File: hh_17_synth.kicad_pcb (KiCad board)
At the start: 2 copper layers, 90 x 40 mm, 0 parts

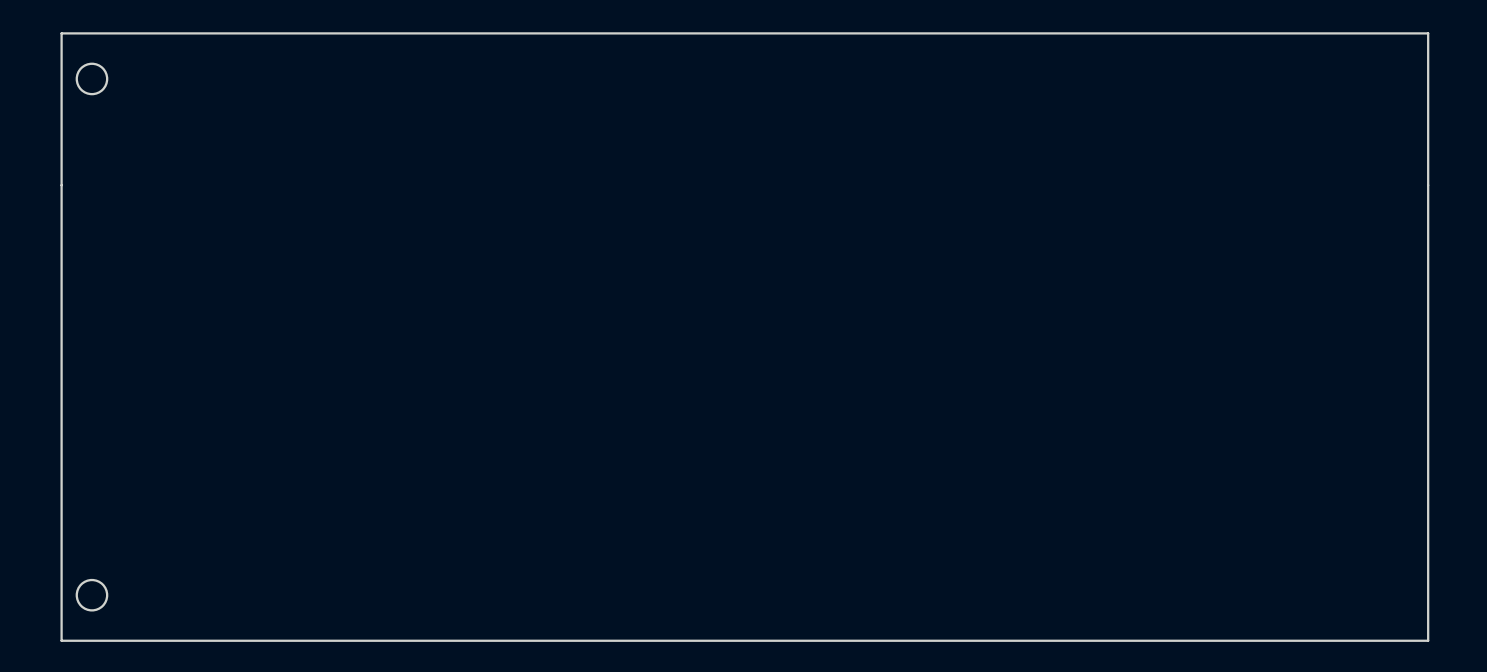
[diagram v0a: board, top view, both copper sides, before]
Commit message: Imported Mitch's touchpad and keyboard lib/mod
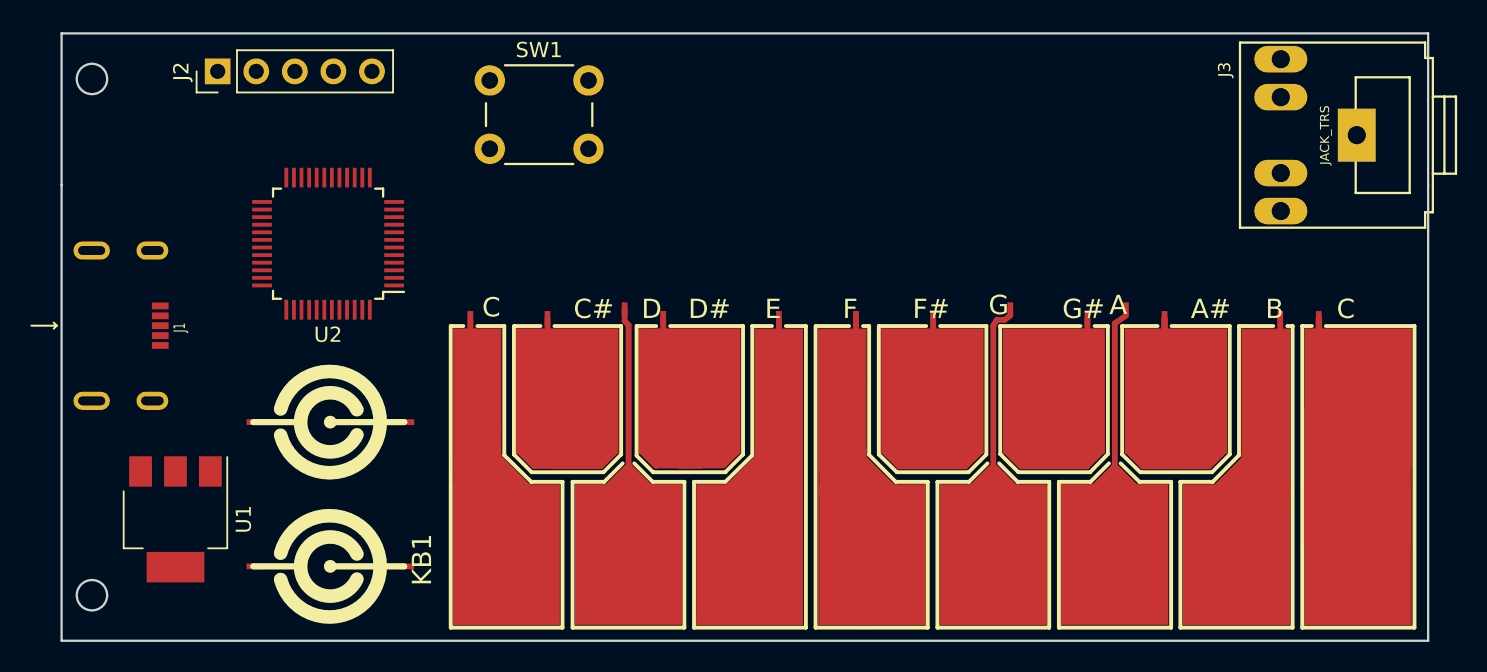
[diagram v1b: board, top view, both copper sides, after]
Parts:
- added J1: USB_OTG, custom:HDMI_476420001_CONN, F.Cu at (71.5, 69.2)
- added J2: debug, Pin_Headers:Pin_Header_Straight_1x05_Pitch2.54mm, F.Cu at (75.3, 52.5)
- added J3: JACK_TRS, custom:Tayda_3.5mm_stereo_TRS_jack_A-853, F.Cu at (148.7, 56.7)
- added KB1: MITCH-PARTS_PCB-KEYBOARD2, custom:MITCH-PARTS_PCB-KEYBOARD2_kicad_fix, F.Cu at (122.4, 79.0)
- added SW1: SW_Push, Buttons_Switches_ThroughHole:SW_PUSH_6mm, F.Cu at (93.2, 53.1)
- added TOUCH1: MITCH-PARTS_PCB-TOUCHPAD2, MITCH-PARTS_PCB-TOUCHPAD2, F.Cu at (82.7, 75.6)
- added TOUCH2: MITCH-PARTS_PCB-TOUCHPAD2, MITCH-PARTS_PCB-TOUCHPAD2, F.Cu at (82.7, 85.1)
- added U1: LM1117-3.3, TO_SOT_Packages_SMD:SOT-223, F.Cu at (72.5, 82.0)
- added U2: STM32F072CBTx, Housings_QFP:LQFP-48_7x7mm_Pitch0.5mm, F.Cu at (82.5, 63.9)
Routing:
- net /D#: track 0.00 -> 20.6 mm
- net /C: track 0.00 -> 20.0 mm
- net /E: track 0.00 -> 17.3 mm
- net /F: track 0.00 -> 17.1 mm
- net /C#: track 0.00 -> 16.6 mm
- net /D: track 0.00 -> 16.3 mm

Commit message: placed parts, changed some footprints.
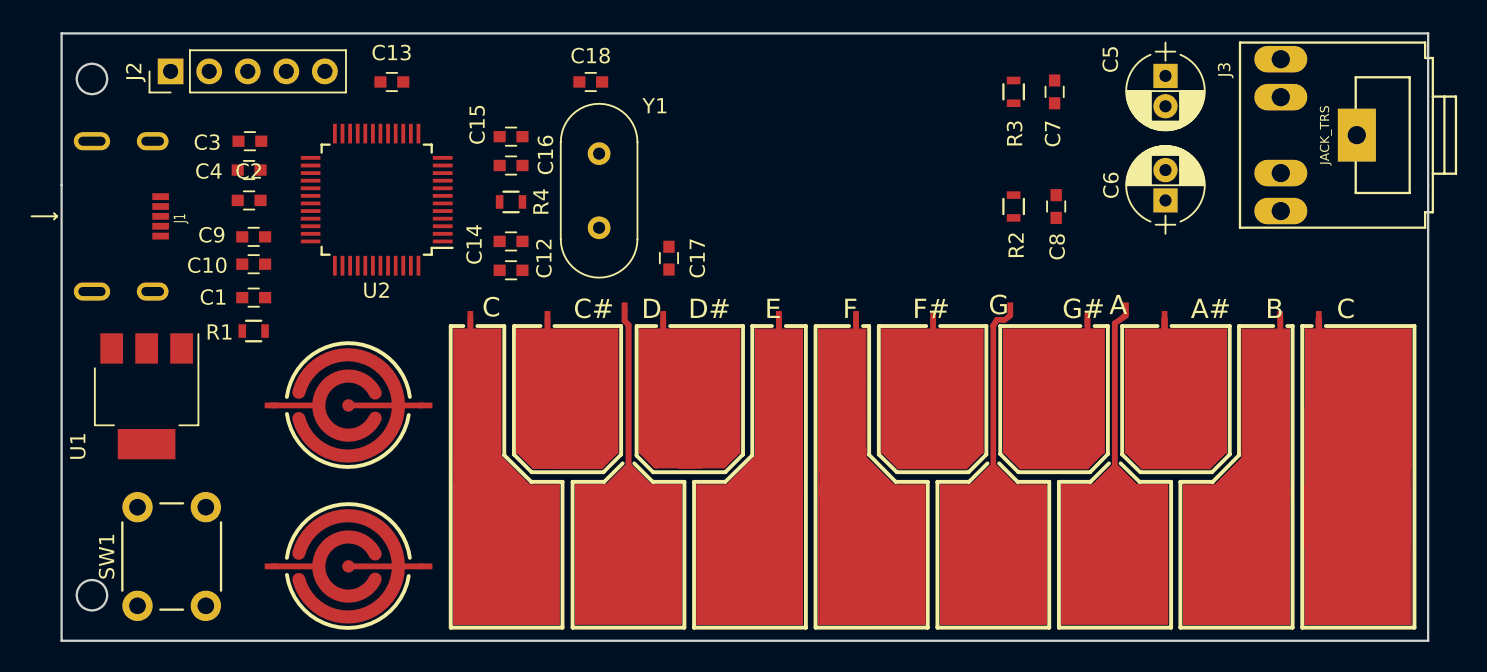
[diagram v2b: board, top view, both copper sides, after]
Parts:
- added C1: 1uF, Capacitors_SMD:C_0603, F.Cu at (77.7, 67.4)
- added C10: 4.7uF, Capacitors_SMD:C_0603, F.Cu at (77.7, 65.2)
- added C12: 100nF, Capacitors_SMD:C_0603, F.Cu at (94.6, 65.6)
- added C13: 100nF, Capacitors_SMD:C_0603, F.Cu at (86.8, 53.2)
- added C14: 4.7uF, Capacitors_SMD:C_0603, F.Cu at (94.6, 63.7)
- added C15: 1uF, Capacitors_SMD:C_0603, F.Cu at (94.6, 56.8)
- added C16: 10nF, Capacitors_SMD:C_0603, F.Cu at (94.6, 58.7)
- added C17: 27pF, Capacitors_SMD:C_0603, F.Cu at (105.0, 64.8)
- added C18: 27pF, Capacitors_SMD:C_0603, F.Cu at (99.8, 53.2)
- added C2: 1uF, Capacitors_SMD:C_0603, F.Cu at (77.3, 61.0)
- added C3: 100nF, Capacitors_SMD:C_0603, F.Cu at (77.4, 57.1)
- added C4: 10nF, Capacitors_SMD:C_0603, F.Cu at (77.3, 59.0)
- added C5: 1uF, Capacitors_ThroughHole:CP_Radial_D5.0mm_P2.00mm, F.Cu at (137.7, 52.8)
- added C6: 1uF, Capacitors_ThroughHole:CP_Radial_D5.0mm_P2.00mm, F.Cu at (137.7, 61.0)
- added C7: 0.1uF, Capacitors_SMD:C_0603, F.Cu at (130.4, 53.9)
- added C8: 0.1uF, Capacitors_SMD:C_0603, F.Cu at (130.5, 61.4)
- added C9: 100nF, Capacitors_SMD:C_0603, F.Cu at (77.7, 63.4)
- added R1: 10k, Resistors_SMD:R_0603, F.Cu at (77.7, 69.6)
- added R2: 8, Resistors_SMD:R_0603, F.Cu at (127.7, 61.4)
- added R3: 8, Resistors_SMD:R_0603, F.Cu at (127.7, 53.9)
- added R4: 220E, Resistors_SMD:R_0603, F.Cu at (94.6, 61.1)
- added Y1: 16MHz, Crystals:Crystal_HC49-4H_Vertical, F.Cu at (100.4, 62.8)
- TOUCH1, TOUCH2: footprint MITCH-PARTS_PCB-TOUCHPAD2 -> custom:MITCH-PARTS_PCB-TOUCHPAD2_kicad_fix
- moved SW1 41.7 mm to (70.0, 87.7), turned to 90 degrees
- moved U1 8.32 mm to (70.6, 73.9)
- moved J1 7.20 mm to (71.5, 62.0)
- moved U2 4.32 mm to (85.8, 61.0)
- moved J2 3.10 mm to (72.2, 52.5)
- moved TOUCH1 1.63 mm to (83.9, 74.5)
- moved TOUCH2 1.20 mm to (83.9, 85.1)
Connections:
- J3 pad 2: (no net) -> Net-(C8-Pad1)
- J3 pad 3: (no net) -> Net-(C7-Pad1)
- U2 pad 14: (no net) -> /DAC_C1
- U2 pad 15: (no net) -> /DAC_C2
- U2 pad 5: (no net) -> /OSC_IN
- U2 pad 6: (no net) -> /OSC_OUT
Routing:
- net /G: track 0.00 -> 16.9 mm
- net /B: track 0.00 -> 16.7 mm
- net /C+: track 0.00 -> 16.7 mm
- net /A: track 0.00 -> 16.5 mm
- net /F#: track 0.00 -> 14.4 mm
- net /A#: track 0.00 -> 13.3 mm
- net /G#: track 0.00 -> 9.46 mm

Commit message: finished layout etc.
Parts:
- moved SW1 15.0 mm to (68.2, 72.8), turned to 0 degrees
- moved U1 11.7 mm to (74.2, 85.0)
- moved C18 6.82 mm to (104.8, 58.0), turned to 90 degrees
- moved R1 5.34 mm to (82.8, 68.2)
- moved C8 3.24 mm to (133.4, 60.0)
- moved R2 3.20 mm to (130.6, 60.0)
- moved C7 2.90 mm to (133.3, 53.9)
- moved R3 2.90 mm to (130.6, 53.9)
- moved C17 1.27 mm to (104.8, 63.5)
- moved C13 1.17 mm to (86.0, 52.4)
- moved C5 0.57 mm to (138.1, 52.4)
- moved C6 0.36 mm to (138.1, 60.9)
- moved J3 0.34 mm to (148.4, 56.5)
- moved C2 0.25 mm to (77.6, 61.0), turned to 180 degrees
- moved C3 0.25 mm to (77.7, 57.1), turned to 180 degrees
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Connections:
- net /USB_DM renamed /USB_D_N
- net /USB_DP renamed /USB_D_P
- R2 pad 2: /DAC_C2 -> /DAC_C1
- R3 pad 2: /DAC_C1 -> /DAC_C2
- SW1 pad 2: Net-(SW1-Pad2) -> /VDD
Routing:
- net /VDD: track 0.00 -> 114.1 mm, vias 0 -> 5
- net /C+: track 16.7 -> 98.4 mm, vias 0 -> 2
- net /B: track 16.7 -> 96.0 mm, vias 0 -> 2
- net /A#: track 13.3 -> 83.4 mm, vias 0 -> 2
- net GND: track 0.00 -> 62.9 mm, vias 0 -> 28
- net /A: track 16.5 -> 79.0 mm, vias 0 -> 2
- net /E: track 17.3 -> 78.7 mm, vias 0 -> 2
- net /G#: track 9.46 -> 69.1 mm, vias 0 -> 2
- net /F: track 17.1 -> 76.2 mm, vias 0 -> 2
- net /G: track 16.9 -> 74.4 mm, vias 0 -> 2
- net /C: track 20.0 -> 77.0 mm, vias 0 -> 2
- net /F#: track 14.4 -> 70.8 mm, vias 0 -> 2
- net /C#: track 16.6 -> 68.3 mm, vias 0 -> 2
- net /D#: track 20.6 -> 72.2 mm, vias 0 -> 2
- net /DAC_C1: track 0.00 -> 46.2 mm
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- added copper zone on B.Cu, net /VBUS
- added copper zone on F.Cu, net /VBUS
- added copper zone on F.Cu, net /VDD
- added copper zone on B.Cu, net GND
- added copper zone on F.Cu, net GND
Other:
- outline, holes or cut-outs redrawn
- net class Default: clearance 0.2 -> 0.15
- rule trace_clearance: 0.2 -> 0.15

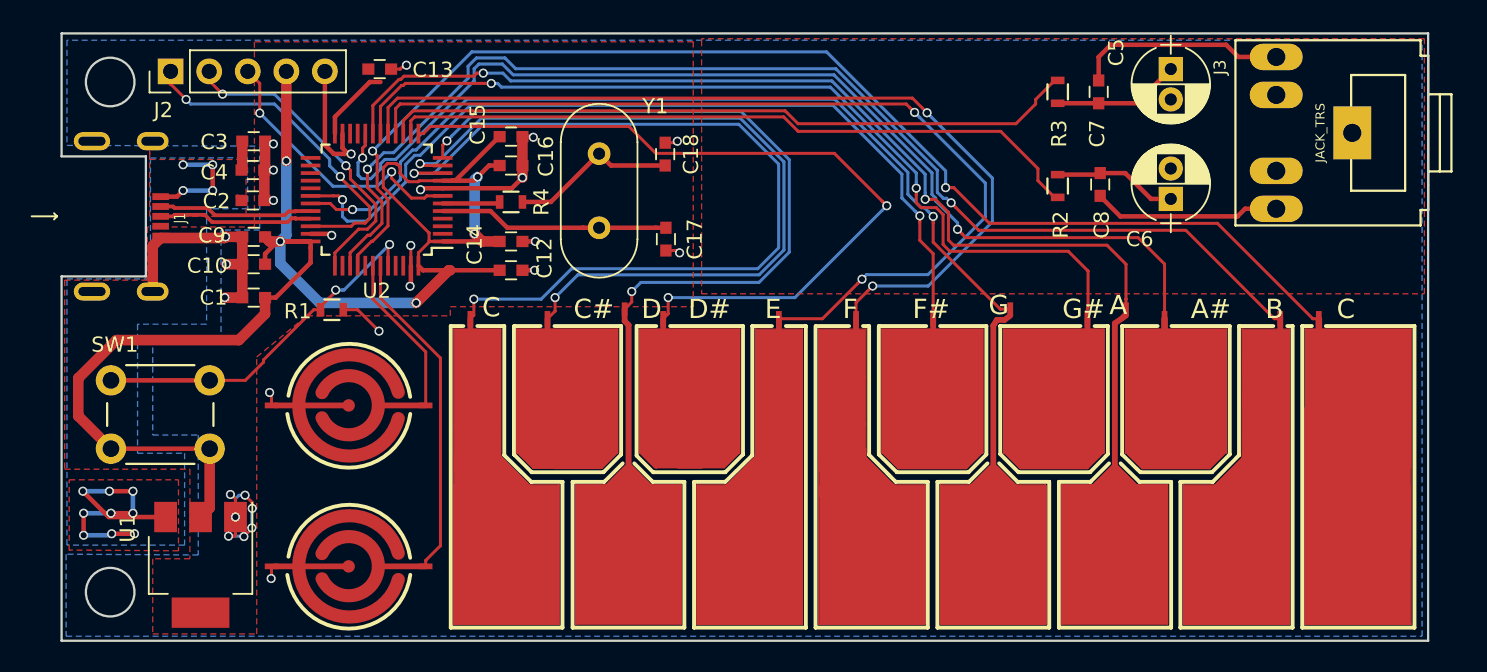
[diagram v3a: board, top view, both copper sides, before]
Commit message: updated layout with buttons/pots
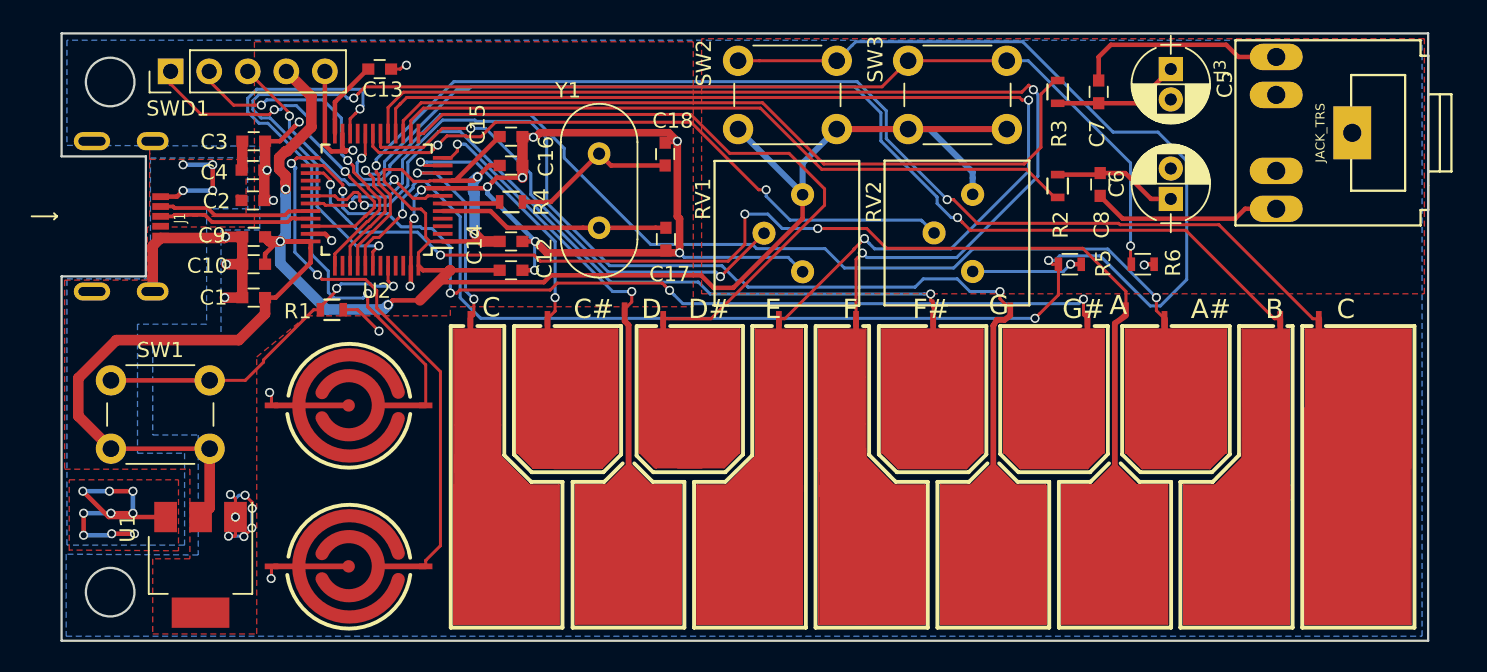
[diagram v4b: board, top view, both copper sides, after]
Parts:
- removed J2: debug, Pin_Headers:Pin_Header_Straight_1x05_Pitch2.54mm
- added R5: 10k, Resistors_SMD:R_0603, F.Cu at (131.4, 65.2)
- added R6: 10k, Resistors_SMD:R_0603, F.Cu at (136.2, 65.2)
- added RV1: POT, custom:3386P-1-T, F.Cu at (112.8, 63.2)
- added RV2: POT, custom:3386P-1-T, F.Cu at (124.0, 63.1)
- added SW2: SW_Push, Buttons_Switches_THT:SW_PUSH_6mm, F.Cu at (109.5, 51.8)
- added SW3: SW_Push, Buttons_Switches_THT:SW_PUSH_6mm, F.Cu at (120.8, 51.8)
- added SWD1: debug, Pin_Headers:Pin_Header_Straight_1x05_Pitch2.54mm, F.Cu at (72.2, 52.5)
- C5, C6: footprint Capacitors_ThroughHole:CP_Radial_D5.0mm_P2.00mm -> Capacitors_THT:CP_Radial_D5.0mm_P2.00mm
- SW1: footprint Buttons_Switches_ThroughHole:SW_PUSH_6mm -> Buttons_Switches_THT:SW_PUSH_6mm
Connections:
- net /VDD renamed VDD
- U2 pad 18: /G# -> /PT1
- U2 pad 19: /A -> /PT2
- U2 pad 22: (no net) -> /TB1
- U2 pad 25: (no net) -> /TB2
- U2 pad 26: (no net) -> /G#
- U2 pad 27: (no net) -> /A
- U2 pad 41: (no net) -> /PB1
- U2 pad 42: /TB1 -> /PB2
- U2 pad 43: /TB2 -> (no net)
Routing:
- net /PB1: track 0.00 -> 112.1 mm, vias 0 -> 3
- net /PB2: track 0.00 -> 84.2 mm, vias 0 -> 3
- net VDD: track 114.1 -> 175.2 mm
- net GND: track 62.9 -> 119.5 mm, vias 28 -> 31
- net /C: track 77.0 -> 34.0 mm
- net /PT2: track 0.00 -> 42.1 mm, vias 0 -> 2
- net /C#: track 68.3 -> 34.4 mm
- net /PT1: track 0.00 -> 32.7 mm, vias 0 -> 2
- net /TB1: track 10.6 -> 38.3 mm, vias 0 -> 2
- net /D: track 61.1 -> 34.8 mm
- net /TB2: track 21.8 -> 34.2 mm, vias 0 -> 2
- net /F: track 76.2 -> 86.3 mm
- net /E: track 78.7 -> 86.7 mm
- net /D#: track 72.2 -> 64.7 mm, vias 2 -> 0
- net /F#: track 70.8 -> 65.6 mm
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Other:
- board text added: "HILLHACKS '17"

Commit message: added audio amp, uart port, leds
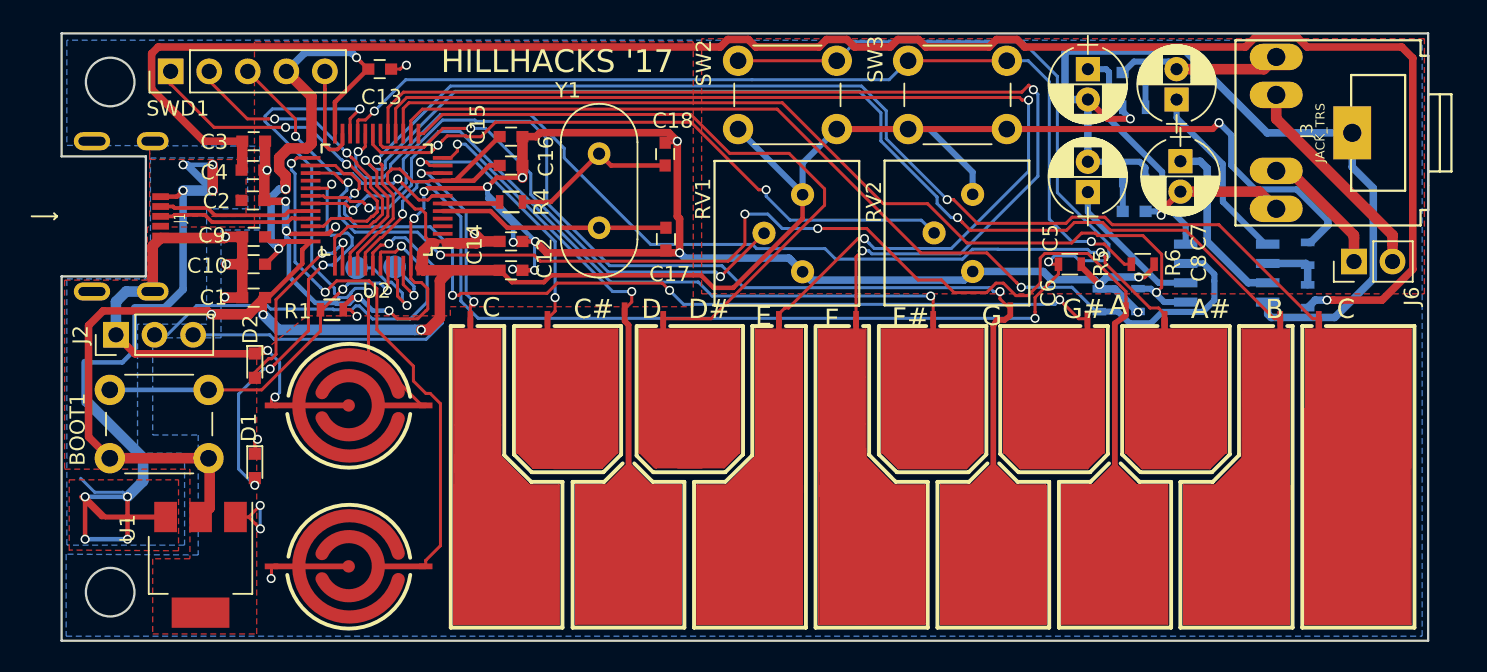
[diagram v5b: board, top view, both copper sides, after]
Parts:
- removed SW1: SW_Push, Buttons_Switches_THT:SW_PUSH_6mm
- added BOOT1: SW_Push, Buttons_Switches_THT:SW_PUSH_6mm, F.Cu at (68.2, 73.5)
- added C11: 0.1uF, Capacitors_SMD:C_0603, B.Cu at (135.6, 52.6)
- added C19: 0.1uF, Capacitors_SMD:C_0603, B.Cu at (135.6, 61.7)
- added D1: LED, LEDs:LED_0603, F.Cu at (77.7, 78.5)
- added D2: LED, LEDs:LED_0603, F.Cu at (77.7, 71.9)
- added J2: serial, Pin_Headers:Pin_Header_Straight_1x03_Pitch2.54mm, F.Cu at (68.6, 69.8)
- added J4: SCL, Measurement_Points:Measurement_Point_Round-SMD-Pad_Small, B.Cu at (84.4, 65.4)
- added J5: SDA, Measurement_Points:Measurement_Point_Round-SMD-Pad_Small, B.Cu at (86.9, 65.4)
- added J6: out, Pin_Headers:Pin_Header_Straight_1x02_Pitch2.54mm, F.Cu at (150.1, 65.0)
- added R10: 4.7, Resistors_SMD:R_0603, B.Cu at (135.6, 59.7)
- added R7: 0E, Resistors_SMD:R_0603, B.Cu at (147.1, 64.5)
- added R8: NC, Resistors_SMD:R_0603, B.Cu at (147.1, 67.3)
- added R9: 4.7, Resistors_SMD:R_0603, B.Cu at (135.6, 54.9)
- added U3: TDA2822, Housings_SOIC:SOIC-8_3.9x4.9mm_Pitch1.27mm, B.Cu at (141.7, 65.8)
- C5, C6: value 1uF -> 100uF
- C7, C8: value 0.1uF -> 470uF; footprint Capacitors_SMD:C_0603 -> Capacitors_THT:CP_Radial_D5.0mm_P2.00mm
- R2, R3: value 8 -> 10k; moved to B.Cu
- moved R3 14.7 mm to (135.9, 67.6), turned to 270 degrees
- moved R2 8.01 mm to (133.3, 67.6), turned to 90 degrees
- moved C8 5.50 mm to (138.7, 58.4), turned to 270 degrees
- moved C6 5.48 mm to (132.6, 60.5)
- moved C5 5.46 mm to (132.6, 52.4)
- moved C7 5.15 mm to (138.4, 54.4), turned to 90 degrees
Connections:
- C7 pad 2: Net-(C5-Pad1) -> /OUT1
- C8 pad 2: Net-(C6-Pad1) -> /OUT2
- J3 pad 2: Net-(C8-Pad1) -> /OUT2
- J3 pad 3: Net-(C7-Pad1) -> /OUT1
- J3 pad 4: (no net) -> Net-(J3-Pad4)
- J3 pad 5: (no net) -> Net-(J3-Pad5)
- R2 pad 1: Net-(C6-Pad1) -> /DAC_C1
- R2 pad 2: /DAC_C1 -> GND
- R3 pad 1: Net-(C5-Pad1) -> /DAC_C2
- R3 pad 2: /DAC_C2 -> GND
- U2 pad 21: (no net) -> /PB2
- U2 pad 29: (no net) -> Net-(D1-Pad2)
- U2 pad 38: (no net) -> Net-(D2-Pad2)
- U2 pad 42: /PB2 -> /TX
- U2 pad 43: (no net) -> /RX
- U2 pad 45: (no net) -> Net-(J4-Pad1)
- U2 pad 46: (no net) -> Net-(J5-Pad1)
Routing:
- net /VBUS: track 29.2 -> 184.2 mm, vias 13 -> 9
- net GND: track 119.5 -> 237.7 mm
- net VDD: track 175.2 -> 207.5 mm, vias 5 -> 8
- net Net-(D1-Pad2): track 0.00 -> 27.6 mm, vias 0 -> 4
- net /TX: track 0.00 -> 27.0 mm, vias 0 -> 1
- net /RX: track 0.00 -> 26.6 mm, vias 0 -> 1
- net /PB2: track 84.2 -> 64.3 mm, vias 3 -> 2
- net /DAC_C1: track 46.2 -> 64.4 mm, vias 0 -> 1
- net Net-(J3-Pad5): track 0.00 -> 14.1 mm
- net Net-(D2-Pad2): track 0.00 -> 13.5 mm, vias 0 -> 2
- net /DAC_C2: track 50.4 -> 63.7 mm, vias 0 -> 1
- net /PB1: track 112.1 -> 99.7 mm
- net /OUT1: track 0.00 -> 11.0 mm
- net /OUT2: track 0.00 -> 9.99 mm, vias 0 -> 1
- net Net-(J3-Pad4): track 0.00 -> 8.61 mm
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
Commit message: changed uart conn to 2 pin (no gnd) misc layout improvements.
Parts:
- J2: footprint Pin_Headers:Pin_Header_Straight_1x03_Pitch2.54mm -> Pin_Headers:Pin_Header_Straight_1x02_Pitch2.54mm
- moved J2 2.54 mm to (71.1, 69.8)
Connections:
- J1 pad 4: (no net) -> Net-(J1-Pad4)
- J2 pad 1: GND -> /RX
- J2 pad 2: /RX -> /TX
- U2 pad 2: (no net) -> Net-(U2-Pad2)
- U2 pad 28: (no net) -> Net-(U2-Pad28)
- U2 pad 3: (no net) -> Net-(U2-Pad3)
- U2 pad 4: (no net) -> Net-(U2-Pad4)
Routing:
- net GND: track 237.7 -> 226.5 mm
- net VDD: track 207.5 -> 208.3 mm, vias 8 -> 9
